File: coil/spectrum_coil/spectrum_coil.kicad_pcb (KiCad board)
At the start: 2 copper layers, 10.7 x 10.7 mm, 1 part, among them T1 Coil

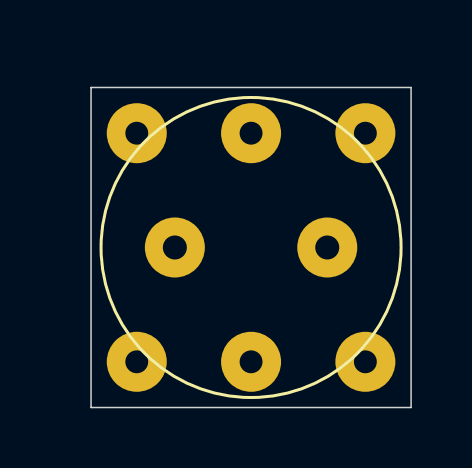
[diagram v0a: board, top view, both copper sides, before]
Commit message: 3d model of the coil
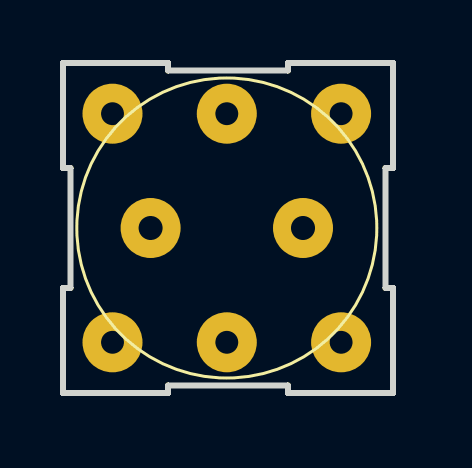
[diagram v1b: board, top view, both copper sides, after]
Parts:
- moved T1 1.04 mm to (119.5, 56.5)
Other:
- board size 10.7 x 10.7 mm -> 11 x 11 mm
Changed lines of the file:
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@@
 	(footprint "ZXSpectrum:Choke"
 		(layer "F.Cu")
-		(at 120.269 57.15)
+		(at 119.46 56.5)
 		(property "Reference" "T1"
 			(at 0 -0.77 0)
@@
 		)
 		(embedded_fonts no)
-	)
-	(gr_rect
-		(start 114.935 51.816)
-		(end 125.603 62.484)
-		(stroke
-			(width 0.05)
-			(type default)
-		)
-		(fill no)
-		(layer "Edge.Cuts")
-	)
+		(model "${KICAD9_3DMODEL_DIR}/Inductor_THT.3dshapes/L_Radial_D8.7mm_P5.00mm_Fastron_07HCP.wrl"
+			(offset
+				(xyz -2.5 0 -0.5)
+			)
+			(scale
+				(xyz 1 1 1)
+			)
+			(rotate
+				(xyz -0 -0 -0)
+			)
+		)
+		(model "${KICAD9_3DMODEL_DIR}/Connector_PinHeader_2.54mm.3dshapes/PinHeader_1x01_P2.54mm_Vertical.step"
+			(offset
+				(xyz 3.8 3.8 -1.5)
+			)
+			(scale
+				(xyz 1 1 1)
+			)
+			(rotate
+				(xyz -0 -180 -0)
+			)
+		)
+		(model "${KICAD9_3DMODEL_DIR}/Connector_PinHeader_2.54mm.3dshapes/PinHeader_1x01_P2.54mm_Vertical.step"
+			(offset
+				(xyz -3.8 3.8 -1.5)
+			)
+			(scale
+				(xyz 1 1 1)
+			)
+			(rotate
+				(xyz -180 -0 -0)
+			)
+		)
+		(model "${KICAD9_3DMODEL_DIR}/Connector_PinHeader_2.54mm.3dshapes/PinHeader_1x01_P2.54mm_Vertical.step"
+			(offset
+				(xyz -3.8 -3.8 -1.5)
+			)
+			(scale
+				(xyz 1 1 1)
+			)
+			(rotate
+				(xyz -180 -0 -0)
+			)
+		)
+		(model "${KICAD9_3DMODEL_DIR}/Connector_PinHeader_2.54mm.3dshapes/PinHeader_1x01_P2.54mm_Vertical.step"
+			(offset
+				(xyz 3.8 -3.8 -1.5)
+			)
+			(scale
+				(xyz 1 1 1)
+			)
+			(rotate
+				(xyz -180 -0 -0)
+			)
+		)
+	)
+	(gr_line
+		(start 121.5 51)
+		(end 125 51)
+		(stroke
+			(width 0.2)
+			(type solid)
+		)
+		(layer "Edge.Cuts")
+	)
+	(gr_line
+		(start 124.75 58.5)
+		(end 125 58.5)
+		(stroke
+			(width 0.2)
+			(type solid)
+		)
+		(layer "Edge.Cuts")
+	)
+	(gr_line
+		(start 121.5 51.25)
+		(end 121.5 51)
+		(stroke
+			(width 0.2)
+			(type solid)
+		)
+		(layer "Edge.Cuts")
+	)
+	(gr_line
+		(start 125 62)
+		(end 121.5 62)
+		(stroke
+			(width 0.2)
+			(type solid)
+		)
+		(layer "Edge.Cuts")
+	)
+	(gr_line
+		(start 125 54.5)
+		(end 124.75 54.5)
+		(stroke
+			(width 0.2)
+			(type solid)
+		)
+		(layer "Edge.Cuts")
+	)
+	(gr_line
+		(start 114 51)
+		(end 117.5 51)
+		(stroke
+			(width 0.2)
+			(type solid)
+		)
+		(layer "Edge.Cuts")
+	)
+	(gr_line
+		(start 114 58.5)
+		(end 114.25 58.5)
+		(stroke
+			(width 0.2)
+			(type solid)
+		)
+		(layer "Edge.Cuts")
+	)
+	(gr_line
+		(start 114.25 54.5)
+		(end 114 54.5)
+		(stroke
+			(width 0.2)
+			(type solid)
+		)
+		(layer "Edge.Cuts")
+	)
+	(gr_line
+		(start 125 51)
+		(end 125 54.5)
+		(stroke
+			(width 0.2)
+			(type solid)
+		)
+		(layer "Edge.Cuts")
+	)
+	(gr_line
+		(start 114 62)
+		(end 114 58.5)
+		(stroke
+			(width 0.2)
+			(type solid)
+		)
+		(layer "Edge.Cuts")
+	)
+	(gr_line
+		(start 124.75 54.5)
+		(end 124.75 58.5)
+		(stroke
+			(width 0.2)
+			(type solid)
+		)
+		(layer "Edge.Cuts")
+	)
+	(gr_line
+		(start 117.5 51.25)
+		(end 121.5 51.25)
+		(stroke
+			(width 0.2)
+			(type solid)
+		)
+		(layer "Edge.Cuts")
+	)
+	(gr_line
+		(start 114 54.5)
+		(end 114 51)
+		(stroke
+			(width 0.2)
+			(type solid)
+		)
+		(layer "Edge.Cuts")
+	)
+	(gr_line
+		(start 121.5 62)
+		(end 121.5 61.75)
+		(stroke
+			(width 0.2)
+			(type solid)
+		)
+		(layer "Edge.Cuts")
+	)
+	(gr_line
+		(start 114.25 58.5)
+		(end 114.25 54.5)
+		(stroke
+			(width 0.2)
+			(type solid)
+		)
+		(layer "Edge.Cuts")
+	)
+	(gr_line
+		(start 117.5 62)
+		(end 114 62)
+		(stroke
+			(width 0.2)
+			(type solid)
+		)
+		(layer "Edge.Cuts")
+	)
+	(gr_line
+		(start 117.5 51)
+		(end 117.5 51.25)
+		(stroke
+			(width 0.2)
+			(type solid)
+		)
+		(layer "Edge.Cuts")
+	)
+	(gr_line
+		(start 125 58.5)
+		(end 125 62)
+		(stroke
+			(width 0.2)
+			(type solid)
+		)
+		(layer "Edge.Cuts")
+	)
+	(gr_line
+		(start 117.5 61.75)
+		(end 117.5 62)
+		(stroke
+			(width 0.2)
+			(type solid)
+		)
+		(layer "Edge.Cuts")
+	)
+	(gr_line
+		(start 121.5 61.75)
+		(end 117.5 61.75)
+		(stroke
+			(width 0.2)
+			(type solid)
+		)
+		(layer "Edge.Cuts")
+	)
